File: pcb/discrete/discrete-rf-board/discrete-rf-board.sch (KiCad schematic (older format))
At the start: 0 parts

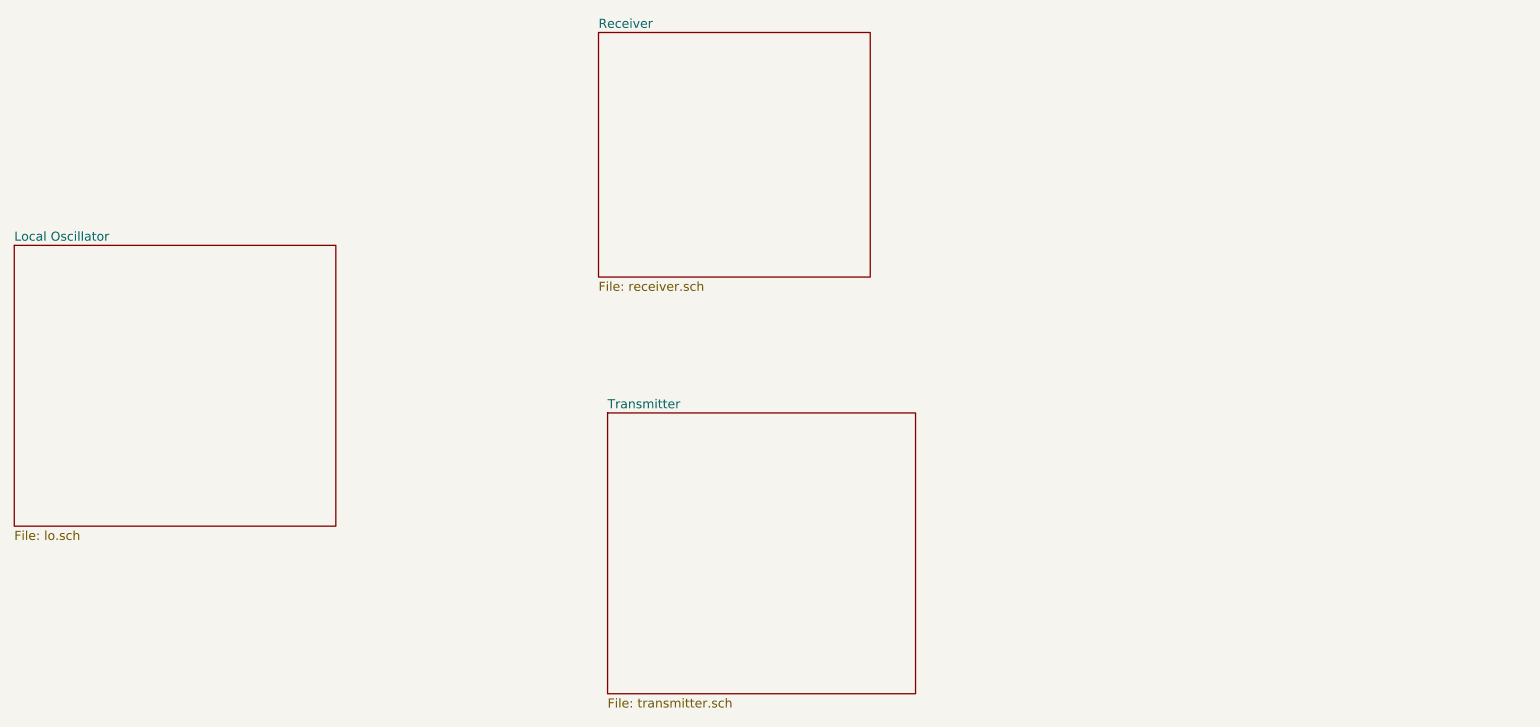
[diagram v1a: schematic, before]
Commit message: Finish active mixer simulation; it looks good!
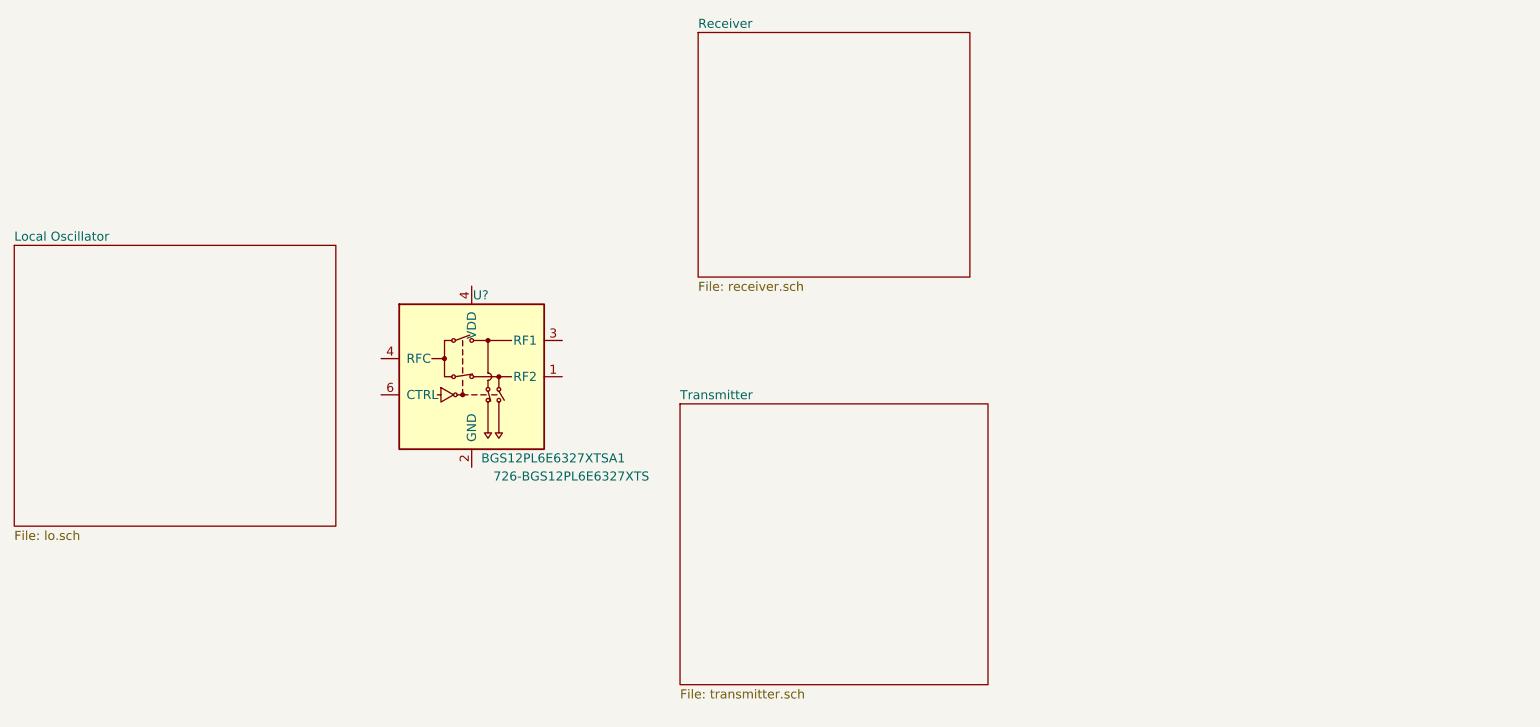
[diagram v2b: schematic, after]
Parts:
- added U?: BGS12PL6E6327XTSA1, symbol discrete-parts:BGS12PL6E6327XTSA1
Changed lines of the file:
@@
 $Descr USLetter 11000 8500
 encoding utf-8
-Sheet 1 4
+Sheet 1 6
 Title ""
 Date ""
@@
 $EndSheet
 $Sheet
-S 5050 1550 1500 1350
+S 5600 1550 1500 1350
 U 5CA6B0AA
 F0 "Receiver" 50
@@
 $EndSheet
 $Sheet
-S 5100 3650 1700 1550
+S 5500 3600 1700 1550
 U 5CA6B0B3
 F0 "Transmitter" 50
 F1 "transmitter.sch" 50
 $EndSheet
+$Comp
+L discrete-parts:BGS12PL6E6327XTSA1 U?
+U 1 1 5CC15EED
+P 4350 3450
+F 0 "U?" H 4400 3900 50  0000 C CNN
+F 1 "BGS12PL6E6327XTSA1" H 4800 3000 50  0000 C CNN
+F 2 "" H 4350 3450 50  0001 C CNN
+F 3 "" H 4350 3450 50  0001 C CNN
+F 4 "726-BGS12PL6E6327XTS" H 4900 2900 50  0000 C CNN "Mouser"
+	1    4350 3450
+	1    0    0    -1
+$EndComp
 $EndSCHEMATC

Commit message: Finish diode mixer simulations and capture in schematic
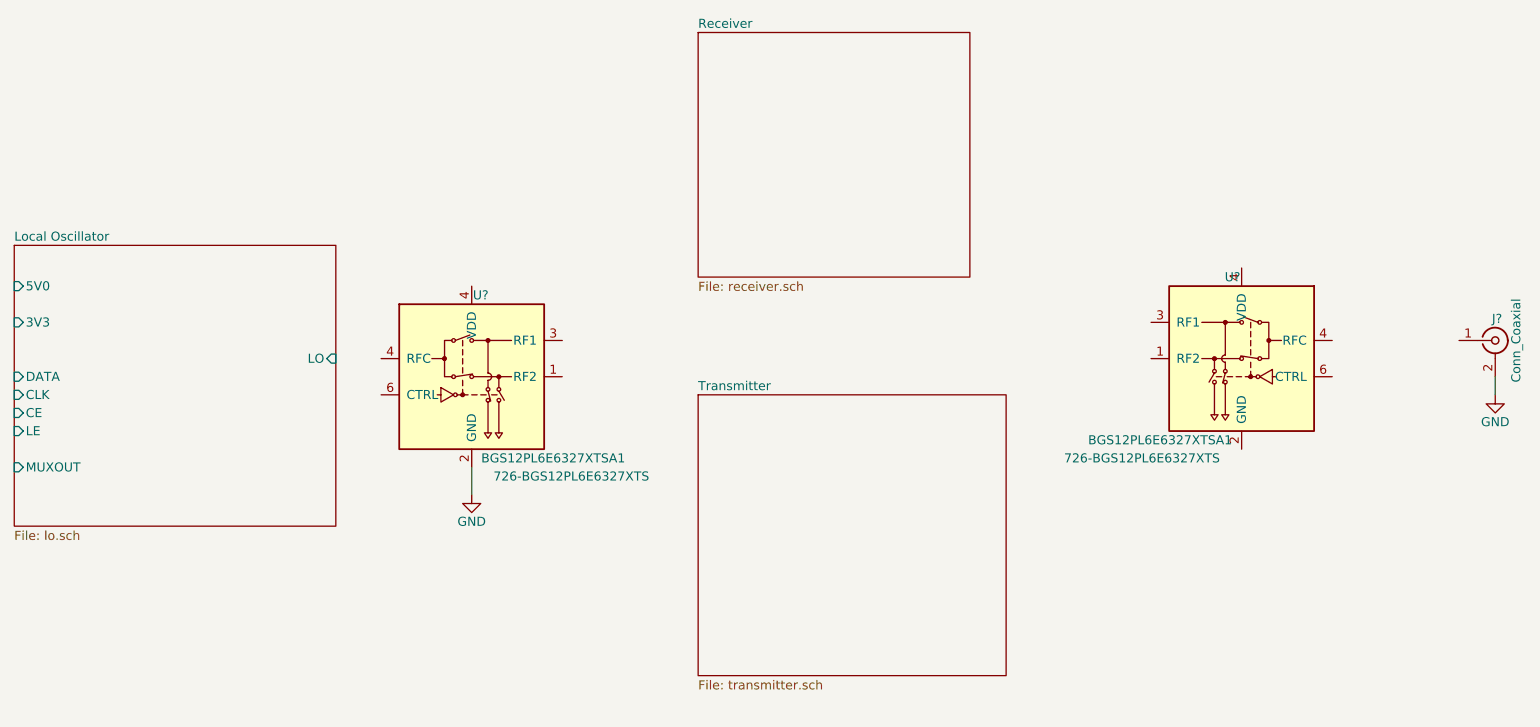
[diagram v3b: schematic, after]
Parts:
- added J?: Conn_Coaxial, symbol Connector:Conn_Coaxial
- added U?: BGS12PL6E6327XTSA1, symbol discrete-parts:BGS12PL6E6327XTSA1
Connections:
- net GND: now reaches U?.2 (GND)
- net GND: now also J?.2 (Ext)
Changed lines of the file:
@@
 $Descr USLetter 11000 8500
 encoding utf-8
-Sheet 1 6
+Sheet 1 8
 Title ""
 Date ""
@@
 $EndDescr
 $Sheet
-S 1825 2725 1775 1550
-U 5CA6B046
-F0 "Local Oscillator" 50
-F1 "lo.sch" 50
-$EndSheet
-$Sheet
 S 5600 1550 1500 1350
 U 5CA6B0AA
@@
 $EndSheet
 $Sheet
-S 5500 3600 1700 1550
+S 5600 3550 1700 1550
 U 5CA6B0B3
 F0 "Transmitter" 50
@@
 	1    0    0    -1
 $EndComp
+$Sheet
+S 1825 2725 1775 1550
+U 5CA6B046
+F0 "Local Oscillator" 50
+F1 "lo.sch" 50
+F2 "CLK" I L 1825 3550 50
+F3 "CE" I L 1825 3650 50
+F4 "MUXOUT" I L 1825 3950 50
+F5 "LE" I L 1825 3750 50
+F6 "DATA" I L 1825 3450 50
+F7 "3V3" I L 1825 3150 50
+F8 "LO" I R 3600 3350 50
+F9 "5V0" I L 1825 2950 50
+$EndSheet
+$Comp
+L power:GND #PWR?
+U 1 1 5CC42654
+P 4350 4100
+F 0 "#PWR?" H 4350 3850 50  0001 C CNN
+F 1 "GND" H 4350 3950 50  0000 C CNN
+F 2 "" H 4350 4100 50  0001 C CNN
+F 3 "" H 4350 4100 50  0001 C CNN
+	1    4350 4100
+	1    0    0    -1
+$EndComp
+Wire Wire Line
+	4350 4100 4350 3950
+$Comp
+L discrete-parts:BGS12PL6E6327XTSA1 U?
+U 1 1 5CC42E59
+P 8600 3350
+F 0 "U?" H 8650 3800 50  0000 C CNN
+F 1 "BGS12PL6E6327XTSA1" H 9050 2900 50  0000 C CNN
+F 2 "" H 8600 3350 50  0001 C CNN
+F 3 "" H 8600 3350 50  0001 C CNN
+F 4 "726-BGS12PL6E6327XTS" H 9150 2800 50  0000 C CNN "Mouser"
+	1    8600 3350
+	-1   0    0    -1
+$EndComp
+$Comp
+L Connector:Conn_Coaxial J?
+U 1 1 5CC44B33
+P 10000 3250
+F 0 "J?" H 10010 3370 50  0000 C CNN
+F 1 "Conn_Coaxial" V 10115 3250 50  0000 C CNN
+F 2 "" H 10000 3250 50  0001 C CNN
+F 3 " ~" H 10000 3250 50  0001 C CNN
+	1    10000 3250
+	1    0    0    -1
+$EndComp
+$Comp
+L power:GND #PWR?
+U 1 1 5CC454AB
+P 10000 3550
+F 0 "#PWR?" H 10000 3300 50  0001 C CNN
+F 1 "GND" H 10000 3400 50  0000 C CNN
+F 2 "" H 10000 3550 50  0001 C CNN
+F 3 "" H 10000 3550 50  0001 C CNN
+	1    10000 3550
+	1    0    0    -1
+$EndComp
+Wire Wire Line
+	10000 3550 10000 3450
 $EndSCHEMATC

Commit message: Capture IF amplifier stages and work on LNA stages
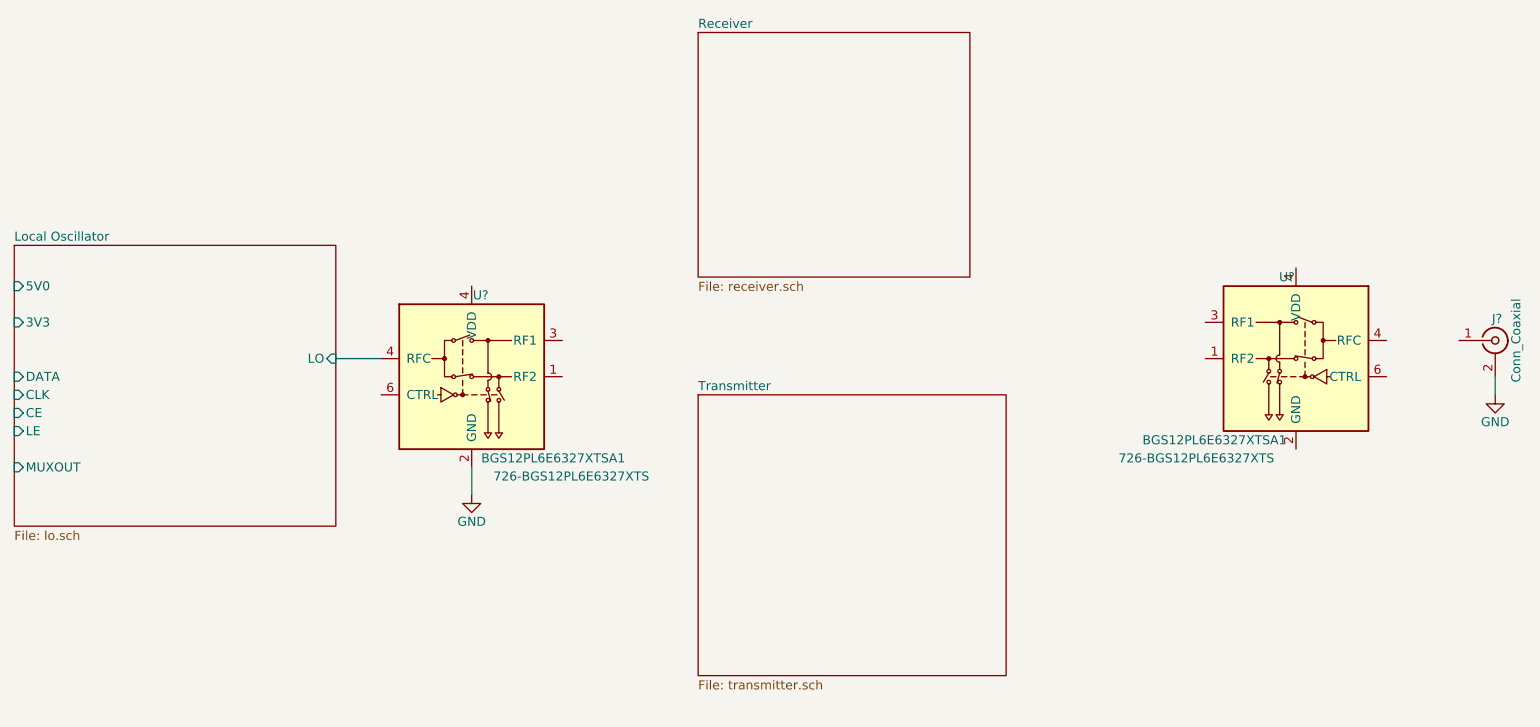
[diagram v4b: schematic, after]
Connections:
- net Local Oscillator/LO: now also U?.4 (VDD)
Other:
- moved on the sheet: U?
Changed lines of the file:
@@
 $Descr USLetter 11000 8500
 encoding utf-8
-Sheet 1 8
+Sheet 1 9
 Title ""
 Date ""
@@
 L discrete-parts:BGS12PL6E6327XTSA1 U?
 U 1 1 5CC42E59
-P 8600 3350
-F 0 "U?" H 8650 3800 50  0000 C CNN
-F 1 "BGS12PL6E6327XTSA1" H 9050 2900 50  0000 C CNN
-F 2 "" H 8600 3350 50  0001 C CNN
-F 3 "" H 8600 3350 50  0001 C CNN
-F 4 "726-BGS12PL6E6327XTS" H 9150 2800 50  0000 C CNN "Mouser"
-	1    8600 3350
+P 8900 3350
+F 0 "U?" H 8950 3800 50  0000 C CNN
+F 1 "BGS12PL6E6327XTSA1" H 9350 2900 50  0000 C CNN
+F 2 "" H 8900 3350 50  0001 C CNN
+F 3 "" H 8900 3350 50  0001 C CNN
+F 4 "726-BGS12PL6E6327XTS" H 9450 2800 50  0000 C CNN "Mouser"
+	1    8900 3350
 	-1   0    0    -1
 $EndComp
@@
 Wire Wire Line
 	10000 3550 10000 3450
+Wire Wire Line
+	3600 3350 3850 3350
 $EndSCHEMATC

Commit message: Save changes while moving over to the new laptop
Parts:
- gave numbers to parts that had none: 3
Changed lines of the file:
@@
 $Descr USLetter 11000 8500
 encoding utf-8
-Sheet 1 9
+Sheet 1 11
 Title ""
 Date ""
@@
 $EndSheet
 $Comp
-L discrete-parts:BGS12PL6E6327XTSA1 U?
+L discrete-parts:BGS12PL6E6327XTSA1 U101
 U 1 1 5CC15EED
 P 4350 3450
-F 0 "U?" H 4400 3900 50  0000 C CNN
+F 0 "U101" H 4400 3900 50  0000 C CNN
 F 1 "BGS12PL6E6327XTSA1" H 4800 3000 50  0000 C CNN
 F 2 "" H 4350 3450 50  0001 C CNN
@@
 $EndSheet
 $Comp
-L power:GND #PWR?
+L power:GND #PWR0101
 U 1 1 5CC42654
 P 4350 4100
-F 0 "#PWR?" H 4350 3850 50  0001 C CNN
+F 0 "#PWR0101" H 4350 3850 50  0001 C CNN
 F 1 "GND" H 4350 3950 50  0000 C CNN
 F 2 "" H 4350 4100 50  0001 C CNN
@@
 	4350 4100 4350 3950
 $Comp
-L discrete-parts:BGS12PL6E6327XTSA1 U?
+L discrete-parts:BGS12PL6E6327XTSA1 U102
 U 1 1 5CC42E59
 P 8900 3350
-F 0 "U?" H 8950 3800 50  0000 C CNN
+F 0 "U102" H 8950 3800 50  0000 C CNN
 F 1 "BGS12PL6E6327XTSA1" H 9350 2900 50  0000 C CNN
 F 2 "" H 8900 3350 50  0001 C CNN
@@
 $EndComp
 $Comp
-L Connector:Conn_Coaxial J?
+L Connector:Conn_Coaxial J101
 U 1 1 5CC44B33
 P 10000 3250
-F 0 "J?" H 10010 3370 50  0000 C CNN
+F 0 "J101" H 10010 3370 50  0000 C CNN
 F 1 "Conn_Coaxial" V 10115 3250 50  0000 C CNN
 F 2 "" H 10000 3250 50  0001 C CNN
@@
 $EndComp
 $Comp
-L power:GND #PWR?
+L power:GND #PWR0102
 U 1 1 5CC454AB
 P 10000 3550
-F 0 "#PWR?" H 10000 3300 50  0001 C CNN
+F 0 "#PWR0102" H 10000 3300 50  0001 C CNN
 F 1 "GND" H 10000 3400 50  0000 C CNN
 F 2 "" H 10000 3550 50  0001 C CNN
